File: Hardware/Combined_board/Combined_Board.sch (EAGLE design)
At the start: 19 parts, among them IC1 788TV, M1 SERVO, M2 SERVO, U1 BMI088

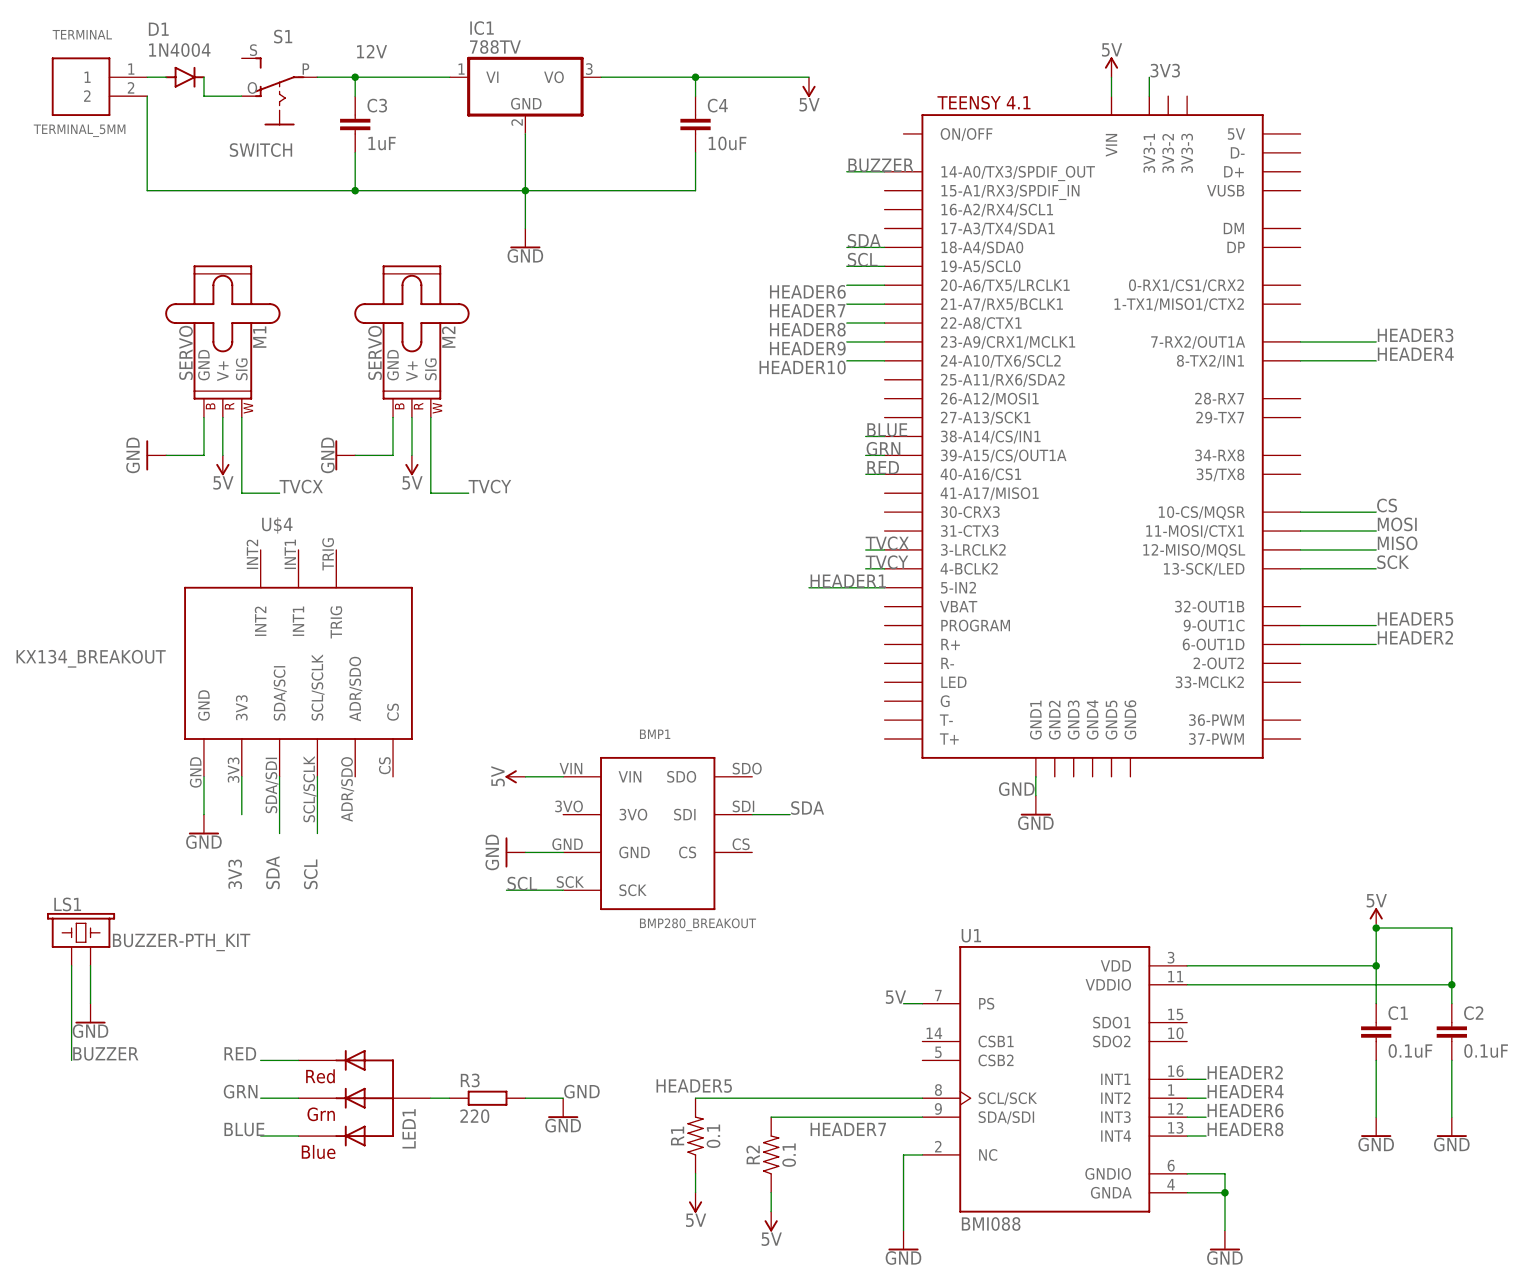
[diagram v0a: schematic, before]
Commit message: added mosfets to combine boards (#56)
* Combined Avionics board and BMI088 board into on PCB named Combined Board, added space for plunger to fit around the combined board. Changed Avionics board to include a diode and power switch.

* added mosfet to combine boards
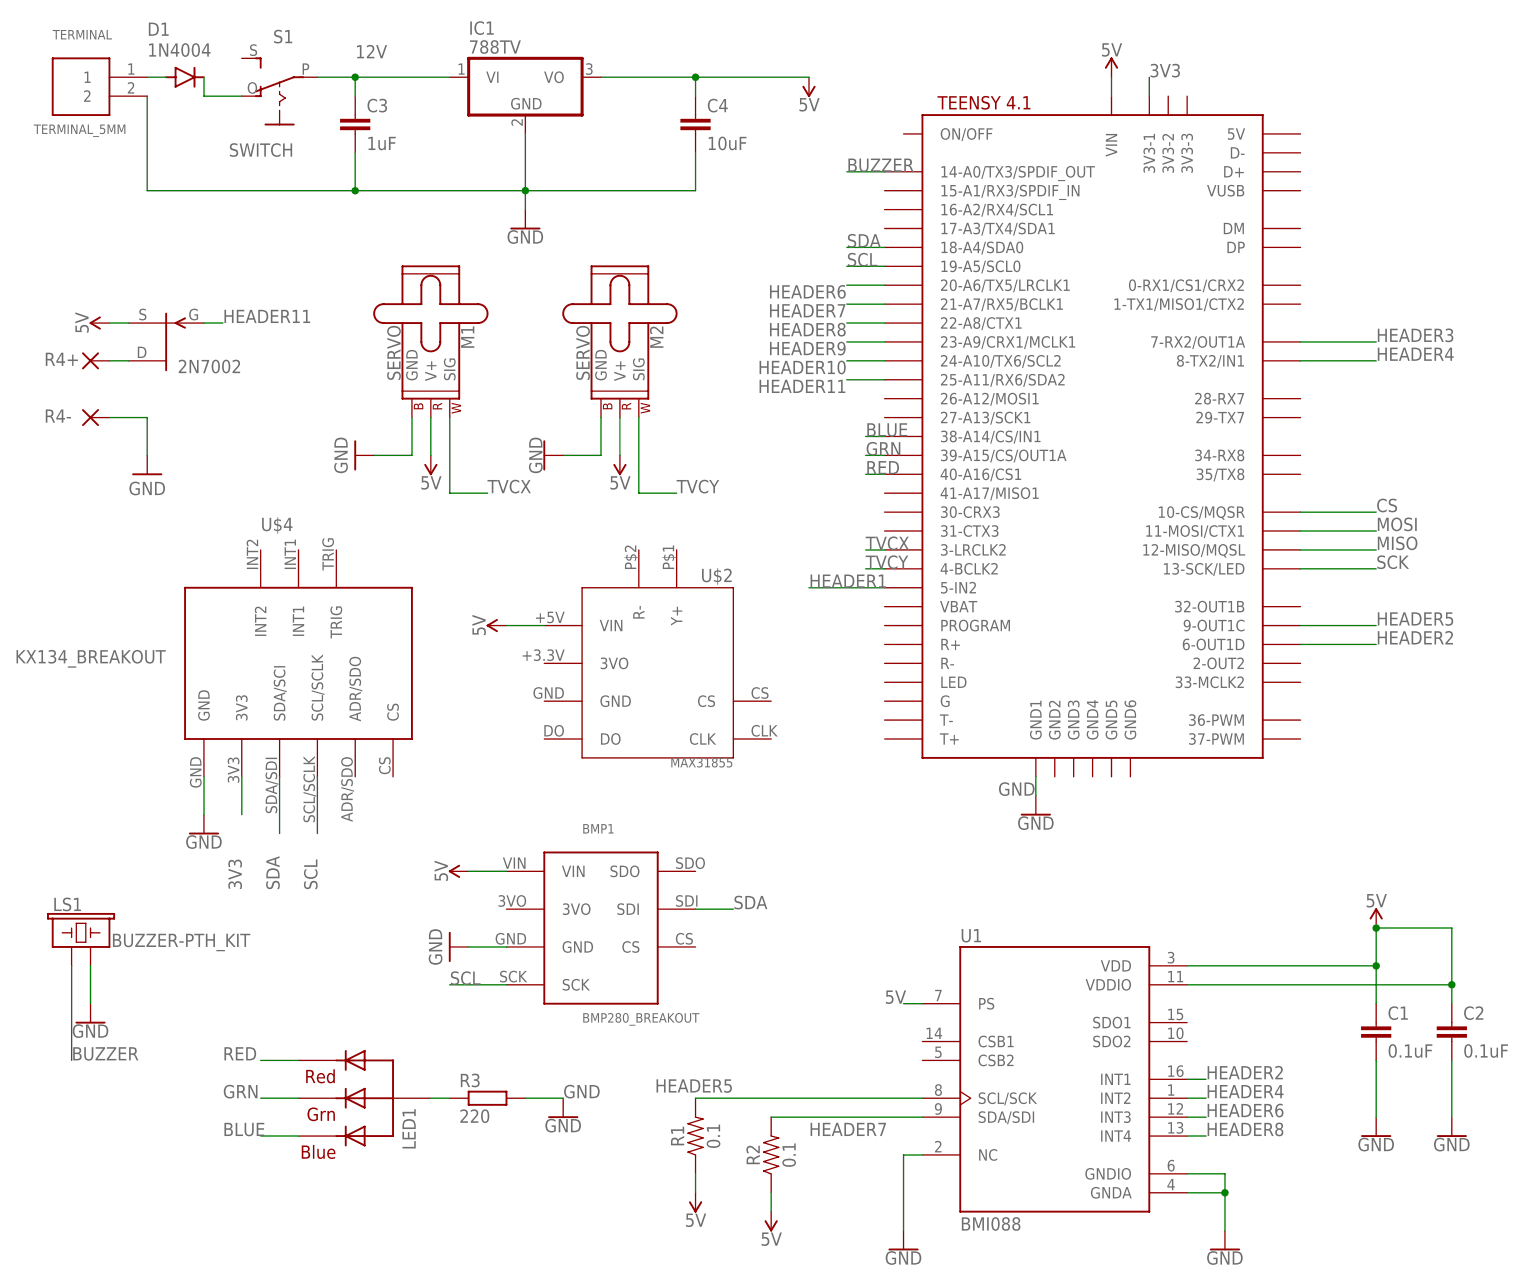
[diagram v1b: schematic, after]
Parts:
- added 2N7002: 2N3819, transistor-fet:2N3819
- added R4+, R4-: (no value), wirepad:1,6/0,8
- added U$2: MAX31855, max31855:MAX31855
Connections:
- new net HEADER11: 2N7002.G, U$1.25-A11/RX6/SDA2
- new net N$3: 2N7002.D, R4+.P
- net 5V: now also 2N7002.S, U$2.VIN
- net GND: now also R4-.P
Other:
- moved on the sheet: BMP1, M1, M2

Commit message: Updated flight computer to new version for mini rockets
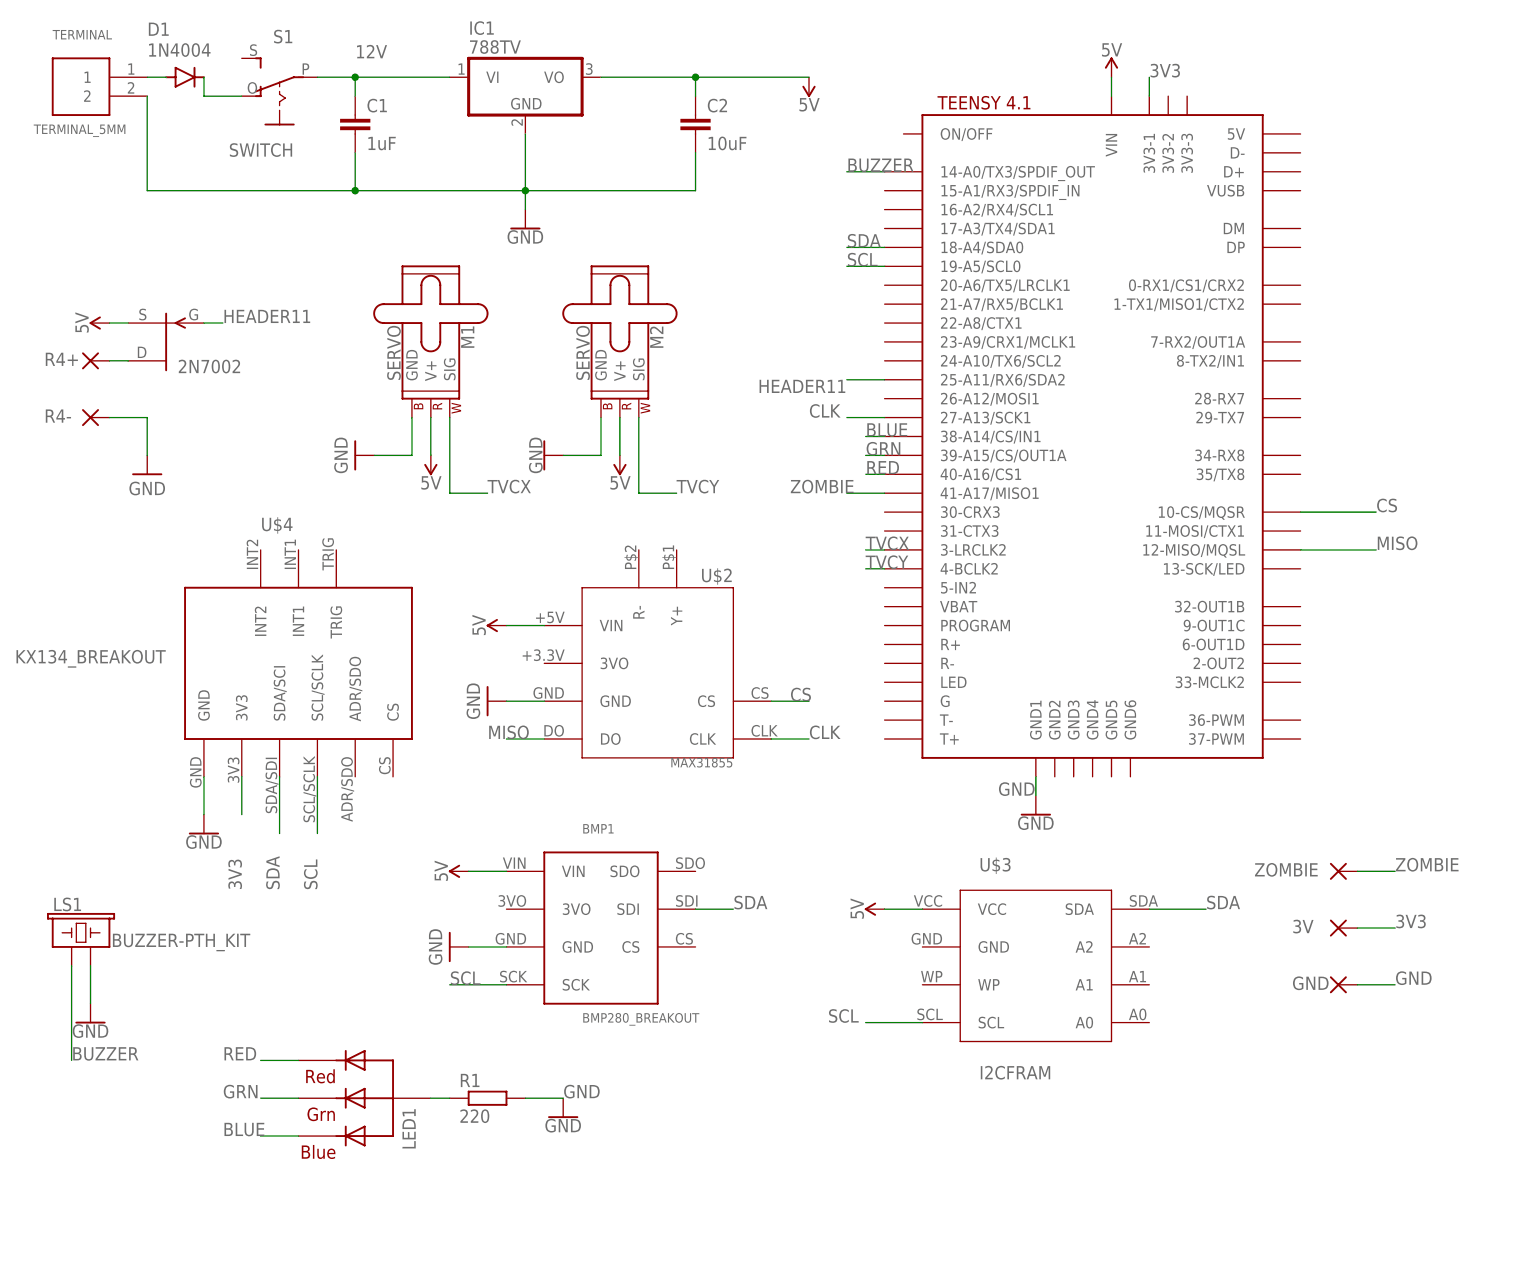
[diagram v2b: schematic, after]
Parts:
- removed C3: 1uF, SparkFun-Capacitors:22PF-PTH-2.54MM-200V-5%
- removed C4: 10uF, SparkFun-Capacitors:22PF-PTH-2.54MM-200V-5%
- removed R2: 0.1, SparkFun-Resistors:0.1OHM-0603-1/3W-1%
- removed R3: 220, rcl:R-EU_0204/7
- removed U1: BMI088, BMI088:BMI088
- added 3V, GND, ZOMBIE: 0, wirepad:1,6/0,8
- added U$3: I2CFRAM, I2CFRAM:I2CFRAM
- C1: value 0.1uF -> 1uF; device SparkFun-Capacitors:0.1UF-0402-16V-10% -> SparkFun-Capacitors:22PF-PTH-2.54MM-200V-5%
- C2: value 0.1uF -> 10uF; device SparkFun-Capacitors:0.1UF-0402-16V-10% -> SparkFun-Capacitors:22PF-PTH-2.54MM-200V-5%
- R1: value 0.1 -> 220; device SparkFun-Resistors:0.1OHM-0603-1/3W-1% -> rcl:R-EU_0204/7
- R4+, R4-: value (none) -> 0
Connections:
- removed net HEADER1: U$1.5-IN2
- removed net HEADER10: U$1.24-A10/TX6/SCL2
- removed net HEADER2: U$1.6-OUT1D, U1.INT1
- removed net HEADER3: U$1.7-RX2/OUT1A
- removed net HEADER4: U$1.8-TX2/IN1, U1.INT2
- removed net HEADER5: R1.2, U$1.9-OUT1C, U1.SCL/SCK
- removed net HEADER6: U$1.20-A6/TX5/LRCLK1, U1.INT3
- removed net HEADER7: R2.2, U$1.21-A7/RX5/BCLK1, U1.SDA/SDI
- removed net HEADER8: U$1.22-A8/CTX1, U1.INT4
- removed net HEADER9: U$1.23-A9/CRX1/MCLK1
- removed net MOSI: U$1.11-MOSI/CTX1
- removed net SCK: U$1.13-SCK/LED
- new net CLK: U$1.27-A13/SCK1, U$2.CLK
- new net ZOMBIE: U$1.41-A17/MISO1, ZOMBIE.P
- net 12V: now also C1.1; no longer C3.1
- net 3V3: now also 3V.P
- net 5V: now also U$3.VCC; no longer C1.1, C4.1, R1.1, R2.1, U1.PS, U1.VDD, U1.VDDIO
- net CS: now also U$2.CS
- net GND: now also GND.P, R1.2, U$2.GND; no longer C3.2, C4.2, R3.2, U1.GNDA, U1.GNDIO, U1.NC
- net MISO: now also U$2.DO
- net N$1: now also R1.1; no longer R3.1
- net SCL: now also U$3.SCL
- net SDA: now also U$3.SDA
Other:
- moved on the sheet: C1, C2
